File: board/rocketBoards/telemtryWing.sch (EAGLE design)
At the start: 22 parts, among them U3 LS20126

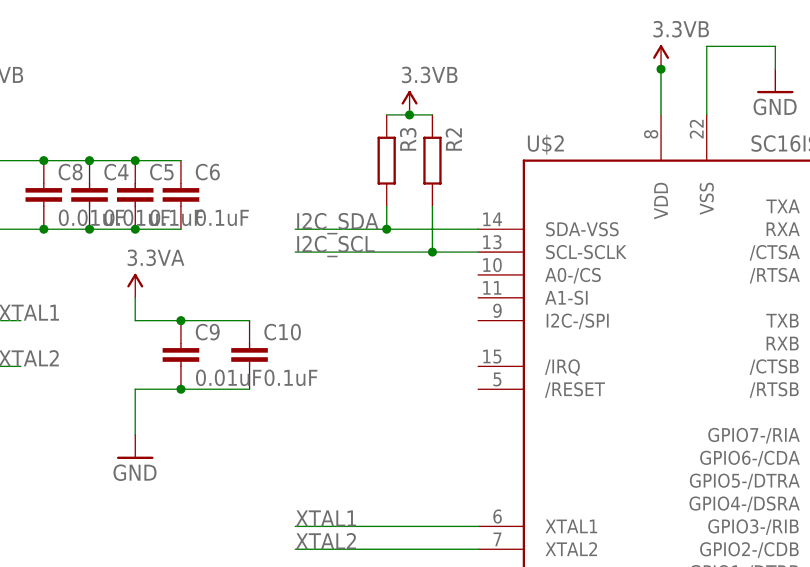
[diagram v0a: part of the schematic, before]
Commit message: added scienceWing
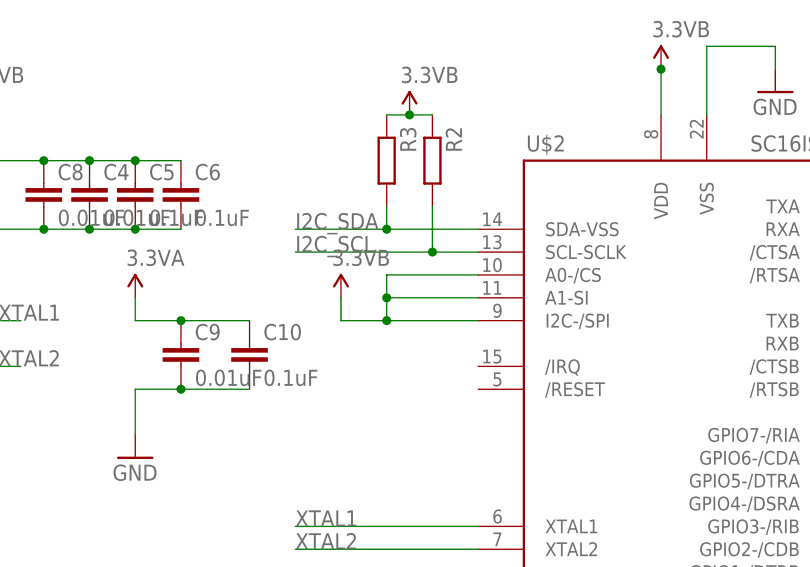
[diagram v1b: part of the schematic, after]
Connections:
- net 3.3V: now also U$2.A0-/CS, U$2.A1-SI, U$2.I2C-/SPI
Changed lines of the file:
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@@
 <part name="SUPPLY2" library="SparkFun-Aesthetics" deviceset="VCC" device="" value="3.3VA"/>
 <part name="GND10" library="SparkFun" deviceset="GND" device=""/>
+<part name="SUPPLY10" library="SparkFun-Aesthetics" deviceset="3.3V" device="" value="3.3VB"/>
 </parts>
 <sheets>
@@
 <instance part="SUPPLY2" gate="G$1" x="17.78" y="96.52"/>
 <instance part="GND10" gate="1" x="17.78" y="78.74"/>
+<instance part="SUPPLY10" gate="G$1" x="40.64" y="96.52"/>
 </instances>
 <busses>
@@
 <pinref part="SUPPLY1" gate="G$1" pin="3.3V"/>
 </segment>
-</net>
+<segment>
+<pinref part="U$2" gate="G$1" pin="I2C-/SPI"/>
+<wire x1="55.88" y1="93.98" x2="45.72" y2="93.98" width="0.1524" layer="91"/>
+<wire x1="45.72" y1="93.98" x2="40.64" y2="93.98" width="0.1524" layer="91"/>
+<wire x1="40.64" y1="93.98" x2="40.64" y2="96.52" width="0.1524" layer="91"/>
+<pinref part="SUPPLY10" gate="G$1" pin="3.3V"/>
+<pinref part="U$2" gate="G$1" pin="A1-SI"/>
+<wire x1="55.88" y1="96.52" x2="45.72" y2="96.52" width="0.1524" layer="91"/>
+<wire x1="45.72" y1="96.52" x2="45.72" y2="93.98" width="0.1524" layer="91"/>
+<junction x="45.72" y="93.98"/>
+<pinref part="U$2" gate="G$1" pin="A0-/CS"/>
+<wire x1="55.88" y1="99.06" x2="45.72" y2="99.06" width="0.1524" layer="91"/>
+<wire x1="45.72" y1="99.06" x2="45.72" y2="96.52" width="0.1524" layer="91"/>
+<junction x="45.72" y="96.52"/>
+</segment>
+</net>
